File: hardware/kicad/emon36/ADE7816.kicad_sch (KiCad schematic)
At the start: 43 parts, among them J15 6_port_3.5mm_audio_jack_array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, J16 6_port_3.5mm_audio_jack_array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, U10 ADE7816

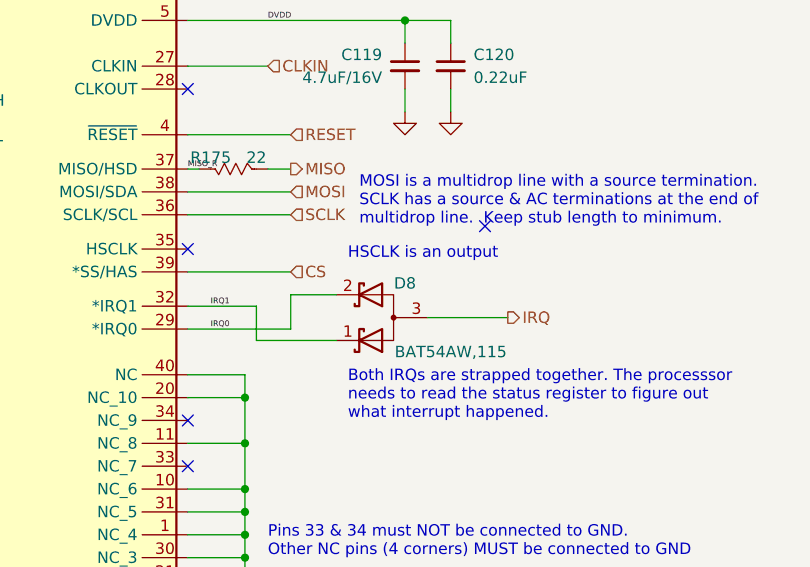
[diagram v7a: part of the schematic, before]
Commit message: Added an optional pullup resistor in case the internal one is not strong enough to boas all the IRQ diodes.
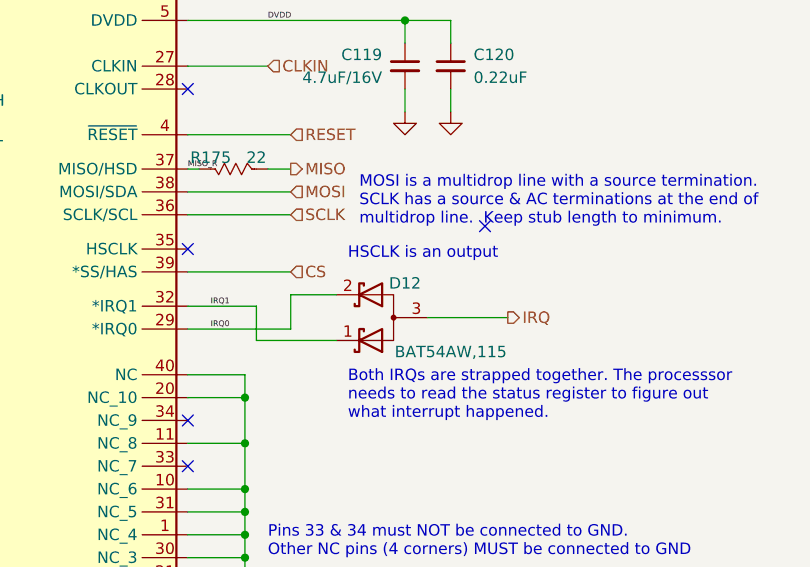
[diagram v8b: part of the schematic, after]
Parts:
- renumbered D8 to D12
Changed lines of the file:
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@@
   (symbol (lib_id "Device:D_Schottky_Dual_CommonAnode_KKA_Parallel") (at 217.17 87.63 180) (unit 1)
     (in_bom yes) (on_board yes)
-    (property "Reference" "D8" (id 0) (at 219.71 83.82 0))
+    (property "Reference" "D12" (id 0) (at 219.71 83.82 0))
     (property "Value" "D_Schottky_Dual_CommonAnode_KKA_Parallel" (id 1) (at 216.8525 81.28 0)
       (effects (font (size 1.27 1.27)) hide)
